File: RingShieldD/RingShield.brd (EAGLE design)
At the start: 70 x 140 mm, 28 parts

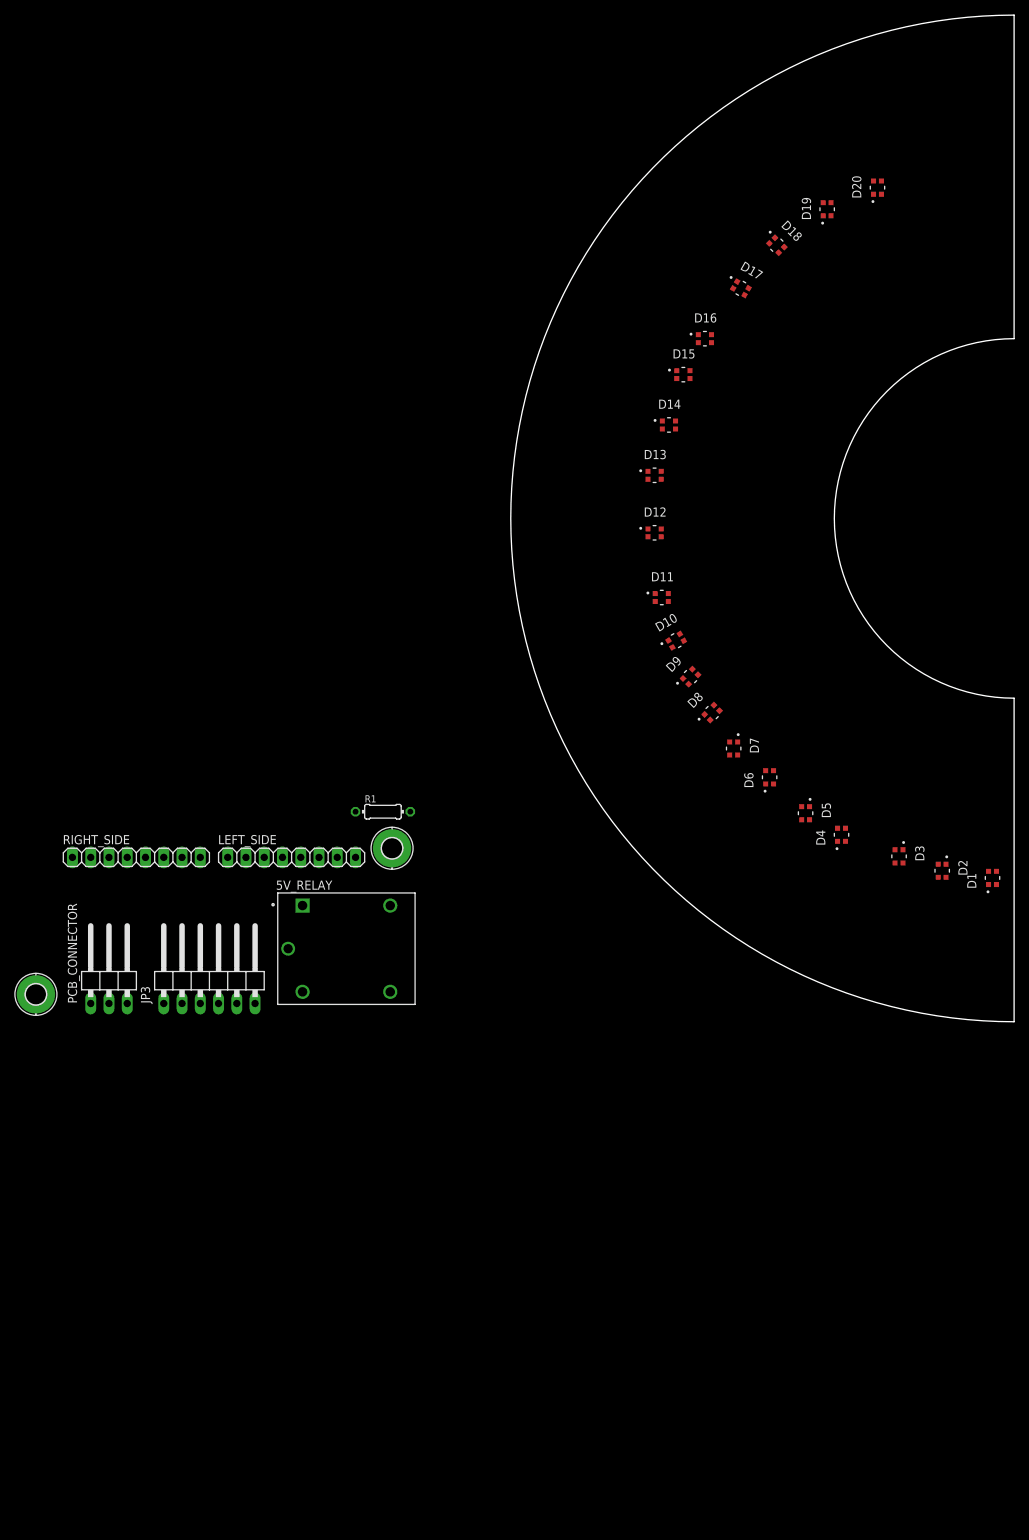
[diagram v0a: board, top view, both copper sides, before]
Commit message: Modifying the layout
Adding 2 folders for 2 pcb, as layout is limiter
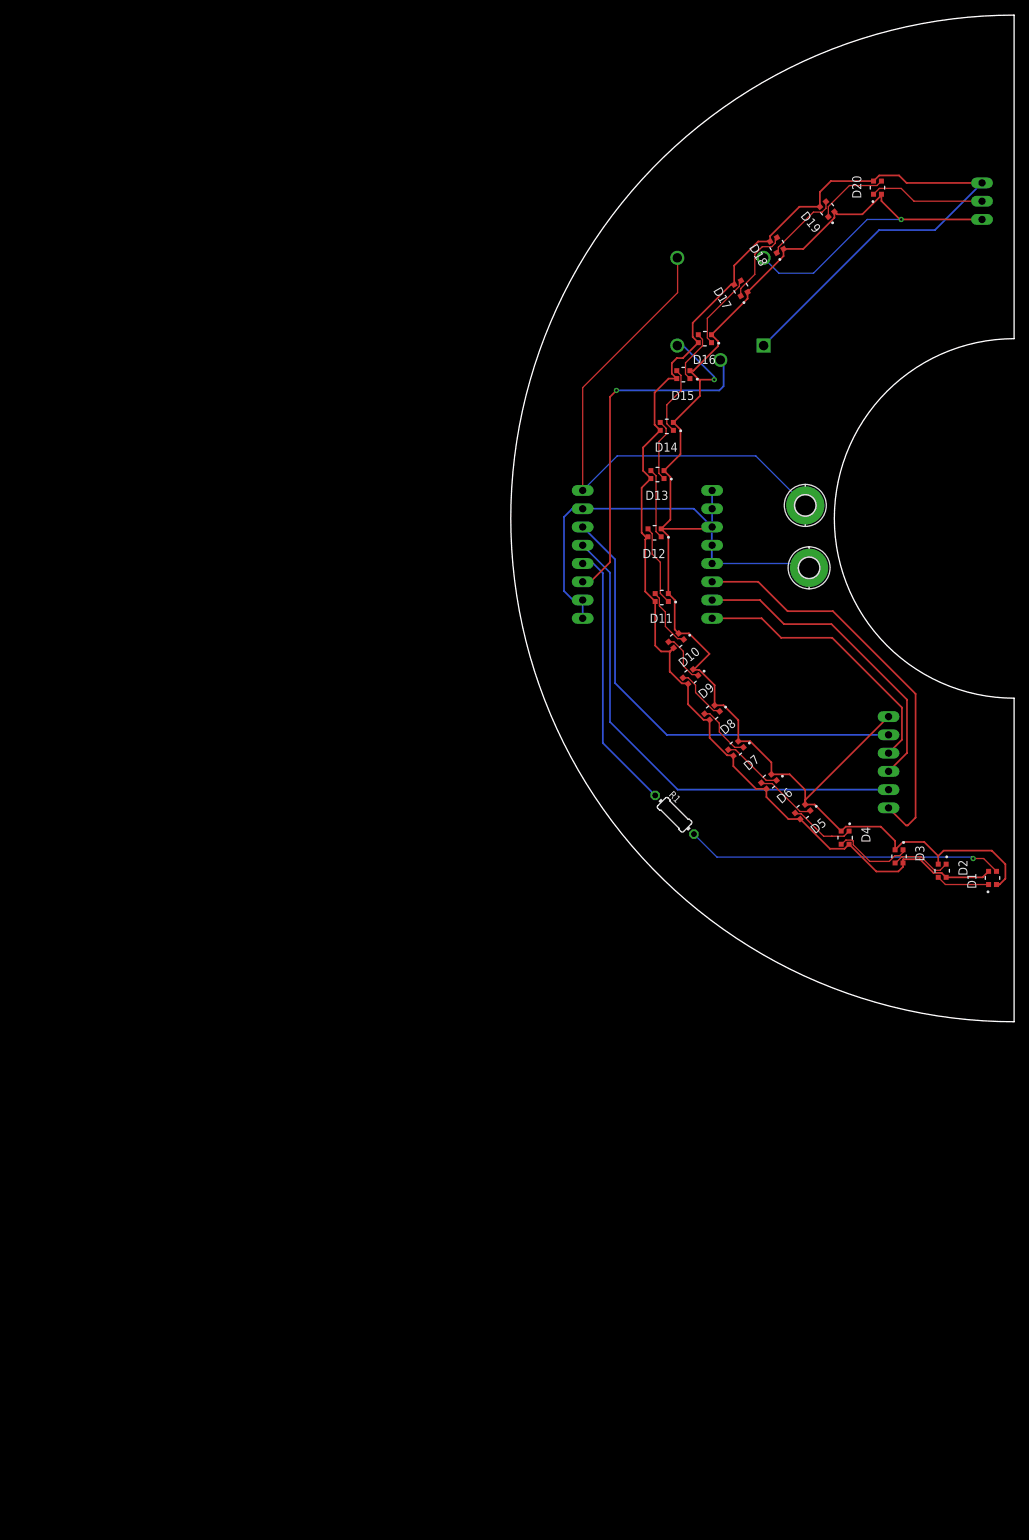
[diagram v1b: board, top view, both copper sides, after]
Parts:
- moved PCB_CONNECTOR 165.2 mm to (69.3, 114.1), flipped to the bottom, turned to 90 degrees
- moved H3 126.8 mm to (41.0, 71.8)
- moved 5V_RELAY 103.9 mm to (29.2, 100.1), flipped to the bottom, turned to 90 degrees
- moved JP3 102.7 mm to (56.4, 36.1), flipped to the bottom, turned to 90 degrees
- moved RIGHT_SIDE 75.0 mm to (10.0, 65.0), flipped to the bottom, turned to 270 degrees
- moved LEFT_SIDE 72.1 mm to (28.0, 65.0), flipped to the bottom, turned to 90 degrees
- moved H4 69.9 mm to (41.5, 63.1)
- moved R1 40.6 mm to (22.8, 28.8), turned to 315 degrees
- moved D4 0.64 mm to (46.5, 25.6), turned to 270 degrees
- moved D6 0.61 mm to (35.9, 33.4), turned to 220 degrees
- moved D5 0.45 mm to (40.6, 29.2), turned to 220 degrees
- moved D13 0.41 mm to (20.4, 76.1), turned to 180 degrees
- moved D14 0.36 mm to (21.7, 82.8), turned to 180 degrees
- moved D7 0.30 mm to (31.3, 38.0), turned to 220 degrees
- turned D10 to 220 degrees
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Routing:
- net GND: track 0.00 -> 294.1 mm, vias 0 -> 2
- net +5V: track 0.00 -> 215.5 mm
- net VIN: track 0.00 -> 73.6 mm
- net SCK: track 0.00 -> 68.8 mm
- net +3V3: track 0.00 -> 64.6 mm
- net CS: track 0.00 -> 57.2 mm
- net CMD: track 0.00 -> 48.2 mm, vias 0 -> 1
- net N$1: track 0.00 -> 44.2 mm, vias 0 -> 1
- net MOSI: track 0.00 -> 43.9 mm
- net MISO: track 0.00 -> 38.7 mm
- net DIN: track 0.00 -> 37.3 mm
- net DO: track 0.00 -> 16.2 mm
- net N$16: track 0.00 -> 11.3 mm
- net N$4: track 0.00 -> 11.3 mm
- net N$19: track 0.00 -> 11.0 mm
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
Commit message: Chagnging right side
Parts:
- removed 5V_RELAY: SRD-05VDC-SL-C, SRD-05VDC-SL-C:RELAY_SRD-05VDC-SL-C
- removed H3, H4: MOUNT-PAD-ROUND2.8, holes:2,8-PAD
- removed JP3: (no value), pinhead:1X06/90
- removed LEFT_SIDE, RIGHT_SIDE: (no value), pinhead:1X08
- removed R1: 330, rcl:0204/7
- moved PCB_CONNECTOR 138.6 mm to (-17.8, 6.35), flipped to the top, turned to 0 degrees
- moved D20 113.5 mm to (-52.1, 68.6), turned to 0 degrees
- moved D2 110.7 mm to (-49.5, 5.08), turned to 0 degrees
- moved D1 103.6 mm to (-35.6, 5.08), turned to 0 degrees
- moved D17 94.1 mm to (-52.1, 59.7), turned to 0 degrees
- moved D19 93.3 mm to (-38.1, 68.6), turned to 0 degrees
- moved D5 92.8 mm to (-52.1, 24.1), turned to 0 degrees
- moved D4 84.6 mm to (-38.1, 24.1), turned to 0 degrees
- moved D8 80.7 mm to (-52.1, 33.0), turned to 0 degrees
- moved D14 80.4 mm to (-52.1, 50.8), turned to 0 degrees
- moved D3 78.1 mm to (-24.1, 24.1), turned to 0 degrees
- moved D11 75.0 mm to (-52.1, 41.9), turned to 0 degrees
- moved D16 74.1 mm to (-38.1, 59.7), turned to 0 degrees
- moved D18 72.7 mm to (-24.1, 68.6), turned to 0 degrees
- moved D7 69.6 mm to (-38.1, 33.0), turned to 0 degrees
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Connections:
- removed net +3V3: JP3.5, RIGHT_SIDE.3
- removed net CMD: 5V_RELAY.COM, RIGHT_SIDE.6
- removed net CS: JP3.1, LEFT_SIDE.3
- removed net DIN: R1.1, RIGHT_SIDE.5
- removed net DO: D20.1, PCB_CONNECTOR.2
- removed net MISO: JP3.4, LEFT_SIDE.1
- removed net MOSI: JP3.3, LEFT_SIDE.2
- removed net SCK: JP3.2, RIGHT_SIDE.4
- removed net VIN: 5V_RELAY.NO, H3.B2,8, RIGHT_SIDE.1
- net +5V: now also PCB_CONNECTOR.1; no longer 5V_RELAY.A1, PCB_CONNECTOR.3
- net GND: now also PCB_CONNECTOR.3; no longer 5V_RELAY.A2, 5V_RELAY.NC, H4.B2,8, JP3.6, LEFT_SIDE.4, LEFT_SIDE.5, LEFT_SIDE.6, LEFT_SIDE.7, LEFT_SIDE.8, PCB_CONNECTOR.1, RIGHT_SIDE.2, RIGHT_SIDE.7, RIGHT_SIDE.8
- net N$1: now also PCB_CONNECTOR.2; no longer R1.2
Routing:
- net GND: track 294.1 -> 0.00 mm, vias 2 -> 0
- net +5V: track 215.5 -> 0.00 mm
- net VIN: track 73.6 -> 0.00 mm
- net SCK: track 68.8 -> 0.00 mm
- net +3V3: track 64.6 -> 0.00 mm
- net CS: track 57.2 -> 0.00 mm
- net CMD: track 48.2 -> 0.00 mm, vias 1 -> 0
- net N$1: track 44.2 -> 0.00 mm, vias 1 -> 0
- net MOSI: track 43.9 -> 0.00 mm
- net MISO: track 38.7 -> 0.00 mm
- net DIN: track 37.3 -> 0.00 mm
- net DO: track 16.2 -> 0.00 mm
- net N$16: track 11.3 -> 0.00 mm
- net N$4: track 11.3 -> 0.00 mm
- net N$19: track 11.0 -> 0.00 mm
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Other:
- outline, holes or cut-outs redrawn

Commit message: Did part D
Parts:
- moved D2 130.7 mm to (17.1, 117.5), turned to 270 degrees
- moved D1 122.5 mm to (10.9, 118.4), turned to 270 degrees
- moved D5 119.4 mm to (34.9, 105.9), turned to 270 degrees
- moved D8 112.7 mm to (47.9, 85.0), turned to 180 degrees
- moved D4 110.2 mm to (29.9, 110.9), turned to 270 degrees
- moved PCB_CONNECTOR 109.4 mm to (0.88, 114.1), turned to 90 degrees
- moved D11 104.3 mm to (49.9, 63.9), turned to 180 degrees
- moved D7 101.8 mm to (44.9, 92.0), turned to 225 degrees
- moved D3 101.8 mm to (23.9, 113.9), turned to 270 degrees
- moved D14 97.1 mm to (44.9, 46.8), turned to 180 degrees
- moved D10 92.7 mm to (49.9, 70.9), turned to 180 degrees
- moved D6 92.7 mm to (39.9, 100.0), turned to 225 degrees
- moved D17 88.8 mm to (32.1, 31.3), turned to 180 degrees
- moved D13 85.0 mm to (46.9, 51.8), turned to 135 degrees
- moved D9 81.4 mm to (48.9, 77.9), turned to 180 degrees
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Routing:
- net GND: track 0.00 -> 187.9 mm
- net +5V: track 0.00 -> 176.8 mm
- net N$19: track 0.00 -> 11.3 mm
- net N$7: track 0.00 -> 10.4 mm
- net N$12: track 0.00 -> 9.74 mm
- net N$3: track 0.00 -> 9.14 mm
- net N$6: track 0.00 -> 8.50 mm
- net N$20: track 0.00 -> 8.48 mm
- net N$5: track 0.00 -> 8.42 mm
- net N$21: track 0.00 -> 8.37 mm
- net N$1: track 0.00 -> 7.77 mm
- net N$11: track 0.00 -> 7.16 mm
- net N$4: track 0.00 -> 7.01 mm
- net N$22: track 0.00 -> 7.00 mm
- net N$13: track 0.00 -> 6.79 mm
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
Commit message: Updating right board
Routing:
- net GND: track 187.9 -> 199.7 mm
- net +5V: track 176.8 -> 184.6 mm
- net N$9: track 6.23 -> 12.1 mm
- net N$10: track 6.38 -> 12.1 mm
- net N$14: track 4.72 -> 10.2 mm
- net N$21: track 8.37 -> 13.8 mm
- net N$5: track 8.42 -> 13.6 mm
- net N$19: track 11.3 -> 16.5 mm
- net N$13: track 6.79 -> 11.6 mm
- net N$4: track 7.01 -> 11.8 mm
- net N$20: track 8.48 -> 13.1 mm
- net N$2: track 6.19 -> 10.7 mm
- net N$6: track 8.50 -> 12.6 mm
- net N$11: track 7.16 -> 11.2 mm
- net N$3: track 9.14 -> 12.9 mm
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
